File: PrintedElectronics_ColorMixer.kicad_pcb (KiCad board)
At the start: 2 copper layers, 148.5 x 105 mm, 5 parts

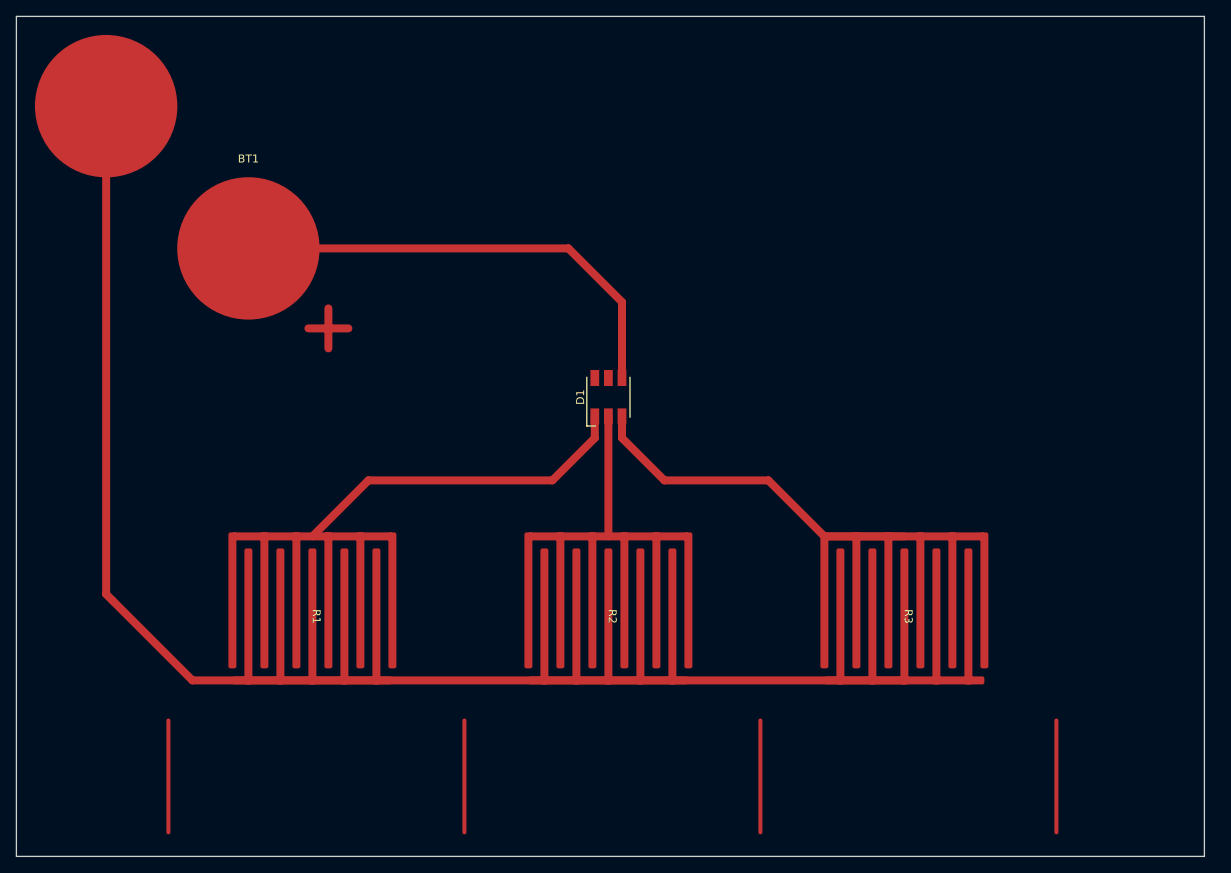
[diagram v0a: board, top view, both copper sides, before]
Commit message: coarser humditiy sensor and bridges for stencils
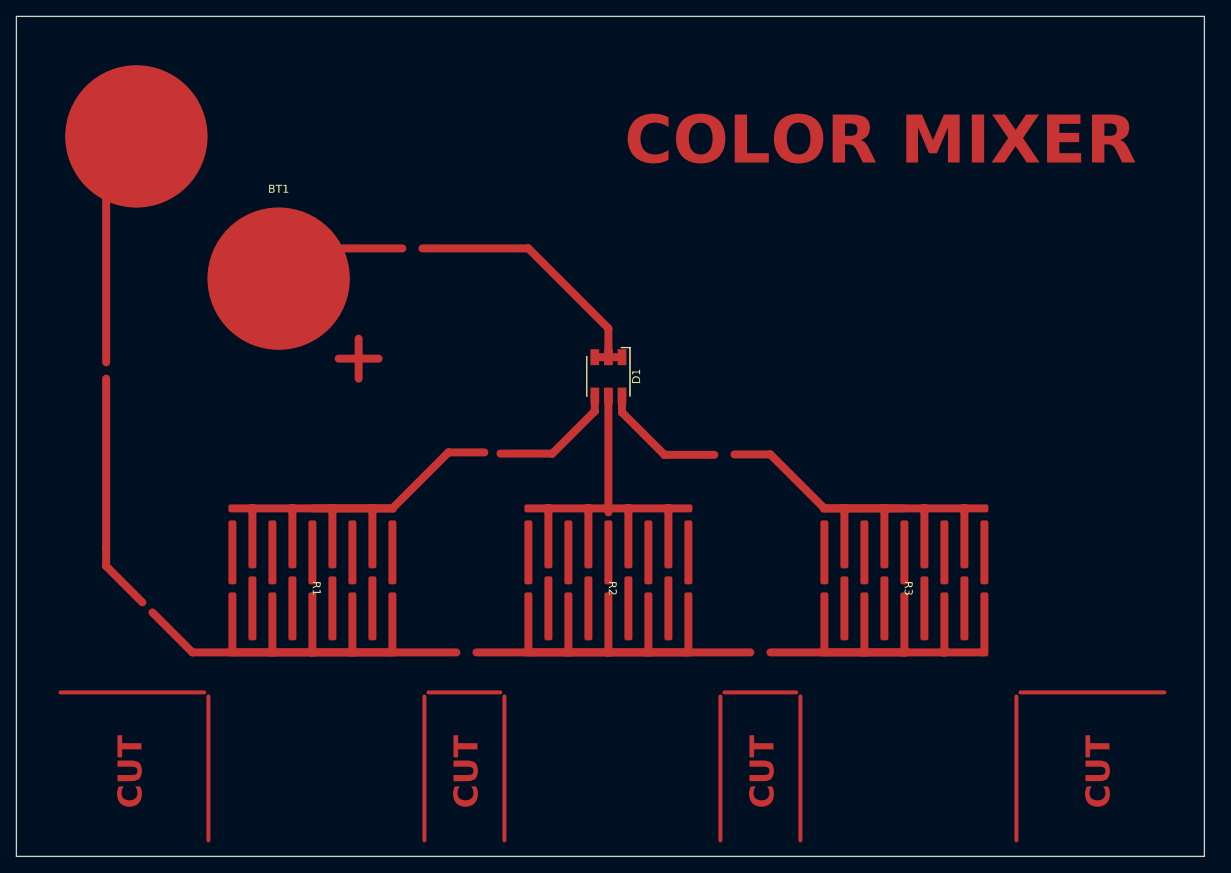
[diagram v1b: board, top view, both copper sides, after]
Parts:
- D1: value LED_RGBK -> LED_RGB
- R1, R2, R3: footprint CHAIR:Humidity_Sensor_Printed_Electronics -> CHAIR:Humidity_Sensor_Printed_Electronics_Stencil
- moved BT1 5.35 mm to (67.8, 77.8)
- moved R1 3.50 mm to (72.0, 116.5)
- moved R2 3.50 mm to (109.0, 116.5)
- moved R3 3.50 mm to (146.0, 116.5)
- moved D1 2.60 mm to (109.0, 90.0), turned to -90 degrees
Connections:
- D1 pad 1: Net-(D1-RA) -> Net-(BT1--)
- D1 pad 2: Net-(D1-GA) -> Net-(BT1--)
- D1 pad 3: Net-(D1-BA) -> Net-(BT1--)
- D1 pad 4: Net-(BT1--) -> Net-(D1-BA)
- D1 pad 5: (no net) -> Net-(D1-GA)
- D1 pad 6: (no net) -> Net-(D1-RA)
- R1 pad 1: Net-(D1-RA) -> Net-(D1-BA)
- R3 pad 1: Net-(D1-BA) -> Net-(D1-RA)
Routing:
- net Net-(BT1-+): track 165.2 -> 152.9 mm
- net Net-(BT1--): track 59.0 -> 53.6 mm
- net Net-(D1-RA): track 43.1 -> 39.9 mm
- net Net-(D1-BA): track 43.1 -> 40.3 mm
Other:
- board text added: "COLOR MIXER"
- board text added: "CUT"
